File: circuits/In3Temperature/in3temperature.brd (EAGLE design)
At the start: 45.4 x 39.3 mm, 24 parts, among them IC1 ATMEGA48/88/168-AU, Q1 MOSFET-NCHANNELSMD, Q2 MOSFET-NCHANNELSMD, Q3 MOSFET-NCHANNELSMD, Q4 MOSFET-NCHANNELSMD, Q5 MOSFET-NCHANNELSMD

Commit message: Electronics v2
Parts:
- removed FAN1, FAN2: (no value), con-amp-quick:02PA
- removed SV1, SV3: (no value), con-lstb:MA06-1
- removed SV2, SV4: (no value), con-lstb:MA04-1
- added C6, C8: 10uf, ng:1206
- added C7: .1uf, ng:1206
- added IC2: REG1117, burr-brown:SOT223
- added R1, R3: 0, ng:1206
- added SL2, SL3: (no value), con-amp-quick:05PA
- added U$3, U$4: AVRISPSMD, 01_FAB_Hello:2X03SMD
- moved C2 21.3 mm to (43.8, 38.3)
- moved C3 21.3 mm to (21.2, 45.1)
- moved C5 21.3 mm to (23.9, 45.1)
- moved LED 21.3 mm to (50.6, 33.8)
- moved Q3 21.3 mm to (28.6, 49.1)
- moved Q4 21.3 mm to (22.7, 52.6)
- moved R7 21.3 mm to (37.8, 40.8)
- moved U$1 21.3 mm to (40.9, 31.0)
- moved C1 21.3 mm to (18.7, 45.1)
- moved C4 21.3 mm to (44.6, 49.8)
- moved IC1 21.3 mm to (30.4, 39.3)
- moved Q1 21.3 mm to (40.8, 22.6)
- moved Q2 21.3 mm to (31.2, 27.2)
- moved Q5 21.3 mm to (37.2, 50.2)
- moved R2 21.3 mm to (47.8, 31.0)
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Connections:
- net 12V: now also C6.2, C7.2, IC2.3, SL2.4, SL3.4, U$3.1; no longer FAN1.1, FAN2.1, SV1.4, SV3.4
- net 5V: now also C8.2, IC2.2, R1.1, R1.2, R3.1, R3.2, U$3.3, U$3.5, U$4.3, U$4.4; no longer SV1.5, SV2.1, SV3.5, SV4.1
- net FAN1O: now also U$3.4, U$3.6; no longer FAN1.2
- net FAN2O: now also U$3.2; no longer FAN2.2
- net GND: now also C6.1, C7.1, C8.1, IC2.1, SL2.5, SL3.5, U$4.1, U$4.2; no longer SV1.6, SV2.4, SV3.6, SV4.4
- net PD3: now also U$4.6; no longer SV2.3
- net PD4: now also U$4.5; no longer SV4.3
- net RST: now also SL2.1, SL3.1; no longer SV1.1, SV3.1
- net SCL: now also SL2.3, SL3.3; no longer SV1.3, SV3.3
- net SDA: now also SL2.2, SL3.2; no longer SV1.2, SV3.2
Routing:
- net 5V: track 166.3 -> 197.0 mm
- net GND: track 205.4 -> 234.0 mm
- net FAN1O: track 8.62 -> 22.0 mm
- net 12V: track 148.1 -> 160.6 mm
- net PD3: track 29.8 -> 17.4 mm
- net FAN2O: track 3.30 -> 12.0 mm
- net PD4: track 20.9 -> 17.9 mm
- net N$3: track 8.30 -> 7.34 mm

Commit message: New Electronics
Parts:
- removed C2: 1uf, ng:1206
- removed C3, C7: .1uf, ng:1206
- removed C4, C5, C6, C8: 10uf, ng:1206
- removed IC1: ATMEGA48/88/168-AU, atmega8:TQFP32-08
- removed IC2: REG1117, burr-brown:SOT223
- removed LED: (no value), ng:1206
- removed R1, R3, R7: 0, ng:1206
- removed R2: 499, ng:1206
- removed SL1: (no value), con-amp-quick:03P
- removed U$4: AVRISPSMD, 01_FAB_Hello:2X03SMD
- added D1, D2, D3: (no value), fab:SOD123
- added J1: (no value), con-jack:SPC4078
- C1: value 1uf -> (none); device ng:1206 -> resistor:E2,5-5
- SL2: device con-amp-quick:05PA -> con-amp-quick:07PA
- SL3: device con-amp-quick:05PA -> con-amp-quick:03P
- U$1: value AVRISPSMD -> RELAY-V23092THROUGH_HOLE; device 01_FAB_Hello:2X03SMD -> 0001_alejandro:RELAY-V23092
- U$2: value RESONATOREFOB -> RELAY-V23092THROUGH_HOLE; device fab:EFOBM -> 0001_alejandro:RELAY-V23092
- moved SL3 44.1 mm to (23.6, 6.60)
- moved PUMP 39.5 mm to (43.4, 15.7), turned to 270 degrees
- moved U$2 37.8 mm to (41.1, 3.81)
- moved U$1 27.8 mm to (35.3, 3.81), turned to 90 degrees
- moved Q1 25.2 mm to (18.1, 33.5)
- moved C1 22.7 mm to (40.1, 37.7), turned to 0 degrees
- moved Q4 19.4 mm to (25.2, 33.4), turned to 180 degrees
- moved Q2 17.8 mm to (14.6, 33.7)
- moved Q3 17.1 mm to (21.7, 33.5), turned to 180 degrees
- moved Q5 15.1 mm to (28.8, 37.6), turned to 270 degrees
- moved SL2 6.50 mm to (17.8, 38.6), turned to 180 degrees
- moved U$3 6.14 mm to (24.1, 19.1)
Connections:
- removed net 5V: C2.2, C3.2, C5.2, C8.2, IC1.18, IC1.20, IC1.4, IC1.6, IC2.2, R1.1, R1.2, R3.1, R3.2, U$1.2, U$3.3, U$3.5, U$4.3, U$4.4
- removed net FAN1: IC1.10, Q1.1
- removed net FAN2: IC1.9, Q2.1
- removed net MISO: IC1.16, U$1.1
- removed net MOSI: IC1.15, U$1.4
- removed net N$1: IC1.8, U$2.1
- removed net N$23: LED.1, R2.2
- removed net N$9: IC1.7, U$2.3
- removed net PD0: IC1.30, Q5.1
- removed net PD3: IC1.1, U$4.6
- removed net PD4: IC1.2, U$4.5
- removed net RST: IC1.29, R7.1, R7.2, SL2.1, SL3.1, U$1.5
- removed net SCK: IC1.17, R2.1, U$1.3
- removed net SCL: IC1.28, SL2.3, SL3.3
- removed net SDA: IC1.27, SL2.2, SL3.2
- new net BLACK: SL3.1, U$2.3
- new net FAN12: Q2.1, SL2.5
- new net FAN5: Q1.1, SL2.4
- new net PUMP: Q5.1, SL2.1
- new net RED: SL3.3, U$1.3
- net 12V: now also C1.+, D1.CATHODE, D2.CATHODE, D3.CATHODE, J1.3, SL2.7, U$1.2, U$1.4, U$2.2, U$2.4, U$3.3, U$3.5; no longer C1.2, C4.2, C6.2, C7.2, IC2.3, SL1.2, SL2.4, SL3.4
- net FAN1O: now also D2.ANODE
- net FAN2O: now also D1.ANODE
- net GND: now also C1.-, J1.1, J1.2, SL2.6, U$1.1, U$2.1; no longer C1.1, C2.1, C3.1, C4.1, C5.1, C6.1, C7.1, C8.1, IC1.21, IC1.3, IC1.5, IC2.1, LED.2, SL2.5, SL3.5, U$1.6, U$2.2, U$4.1, U$4.2
- net N$3: now also D3.ANODE
- net RELAY1: now also SL2.3; no longer IC1.31
- net RELAY1O: now also U$1.5; no longer SL1.3
- net RELAY2: now also SL2.2; no longer IC1.32
- net RELAY2O: now also U$2.5; no longer SL1.1
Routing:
- net GND: track 234.0 -> 0.00 mm
- net 5V: track 197.0 -> 0.00 mm
- net RST: track 66.0 -> 0.00 mm
- net 12V: track 160.6 -> 99.7 mm
- net SDA: track 60.3 -> 0.00 mm
- net SCL: track 60.2 -> 0.00 mm
- net N$3: track 7.34 -> 38.2 mm
- net FAN1: track 19.7 -> 0.00 mm
- net BLACK: track 0.00 -> 19.3 mm
- net PD4: track 17.9 -> 0.00 mm
- net PD3: track 17.4 -> 0.00 mm
- net SCK: track 17.1 -> 0.00 mm
- net MISO: track 16.4 -> 0.00 mm
- net PD0: track 12.7 -> 0.00 mm
- net RED: track 0.00 -> 12.2 mm
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- added copper zone on layer 1, net GND
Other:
- board size 45.4 x 39.3 mm -> 66.5 x 61.2 mm
- board text added: "R"

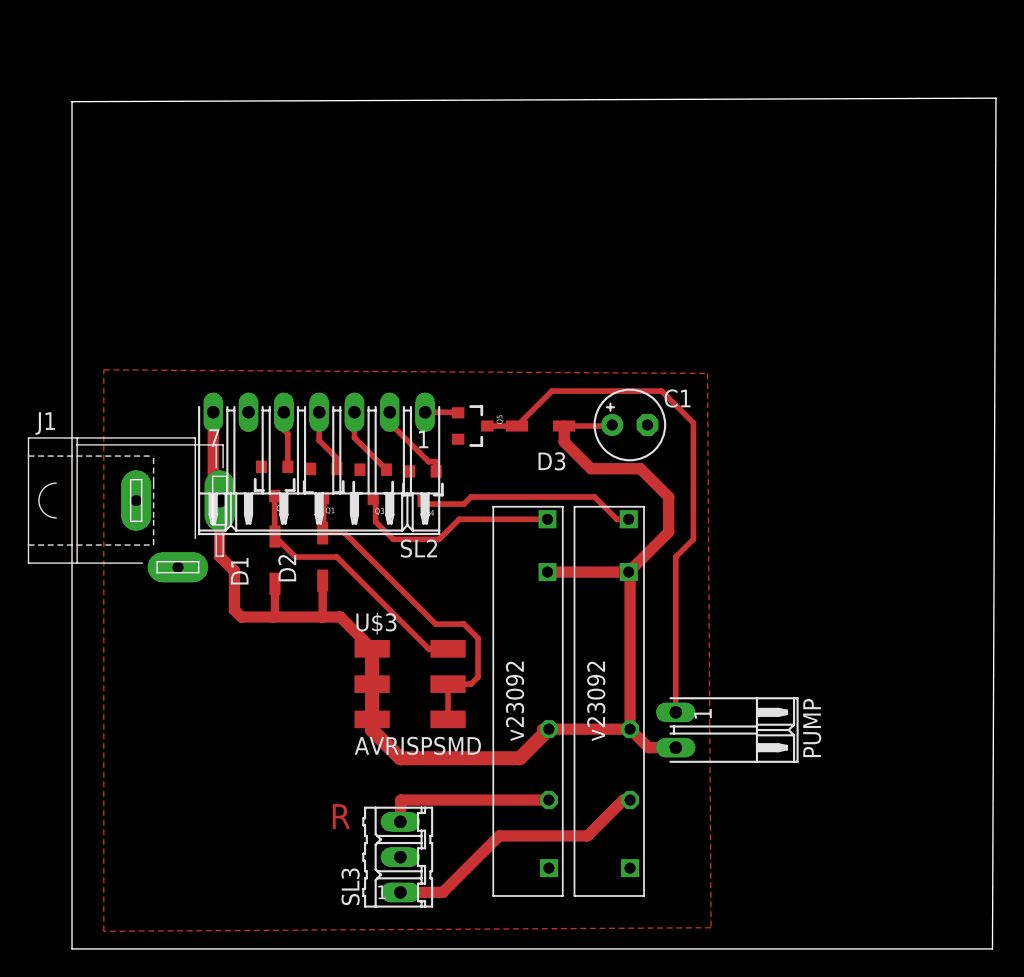
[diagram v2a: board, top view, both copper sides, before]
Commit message: Circuit error fix & improved temperature selector
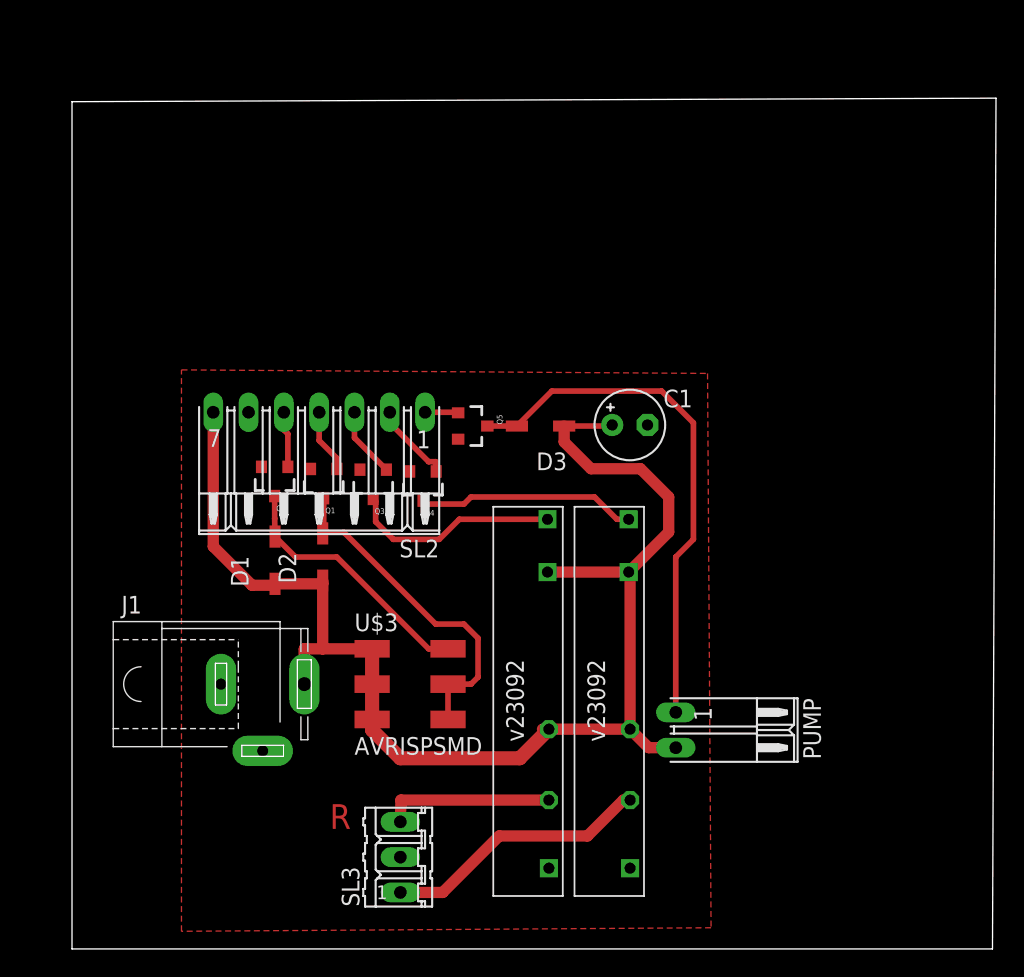
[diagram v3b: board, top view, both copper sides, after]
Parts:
- moved J1 14.5 mm to (13.7, 19.1)
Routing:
- net 12V: track 99.7 -> 102.5 mm
